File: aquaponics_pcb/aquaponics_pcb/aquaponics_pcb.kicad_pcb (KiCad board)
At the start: 2 copper layers, 60.5 x 73.5 mm, 67 parts, among them IC1 AZ1117CH-3.3TRG1, IC2 ESP32-S3-WROOM-1U-N8, IC3 ADM3260ARSZ, IC4 DRV8214RTER, IC5 DRV8214RTER, J1 RFPC-SMA27-F, J2 2338792-1, J3 RFPC-SMA27-F, J4 RFPC-SMA27-F, J5 Screw_Terminal_01x02, J6 Screw_Terminal_01x02, Q1 SSM6N35AFE,LF, Q2 SSM6N35AFE,LF, U1 Atlas Scientific EZO, U2 Atlas Scientific EZO, U3 Atlas Scientific EZO

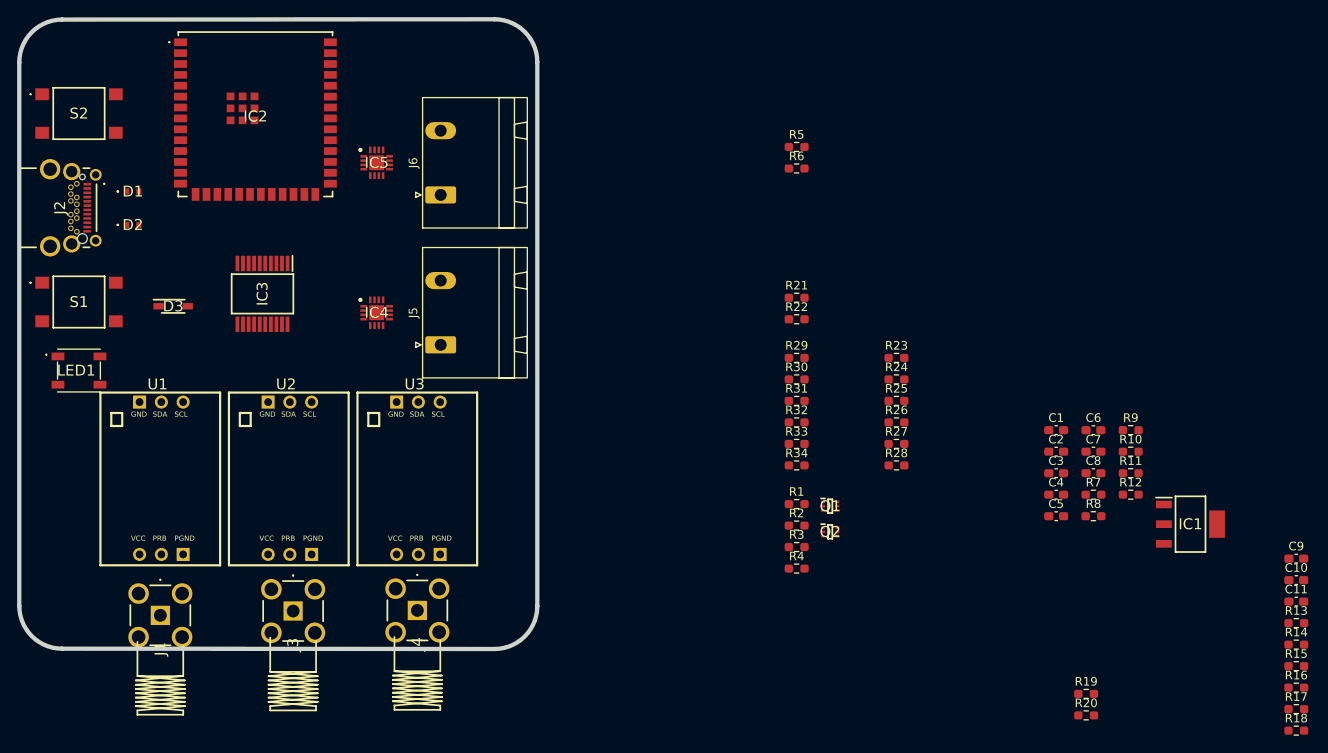
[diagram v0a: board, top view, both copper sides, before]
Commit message: Update PCB: add ADM3260, replace C3 with SMA connector
Replaced C3 capacitor footprint with an RFPC-SMA27-F SMA connector and added the ADM3260ARSZ digital isolator (IC3) to the PCB. Updated R3 to a 10k resistor and made related netlist and footprint changes.
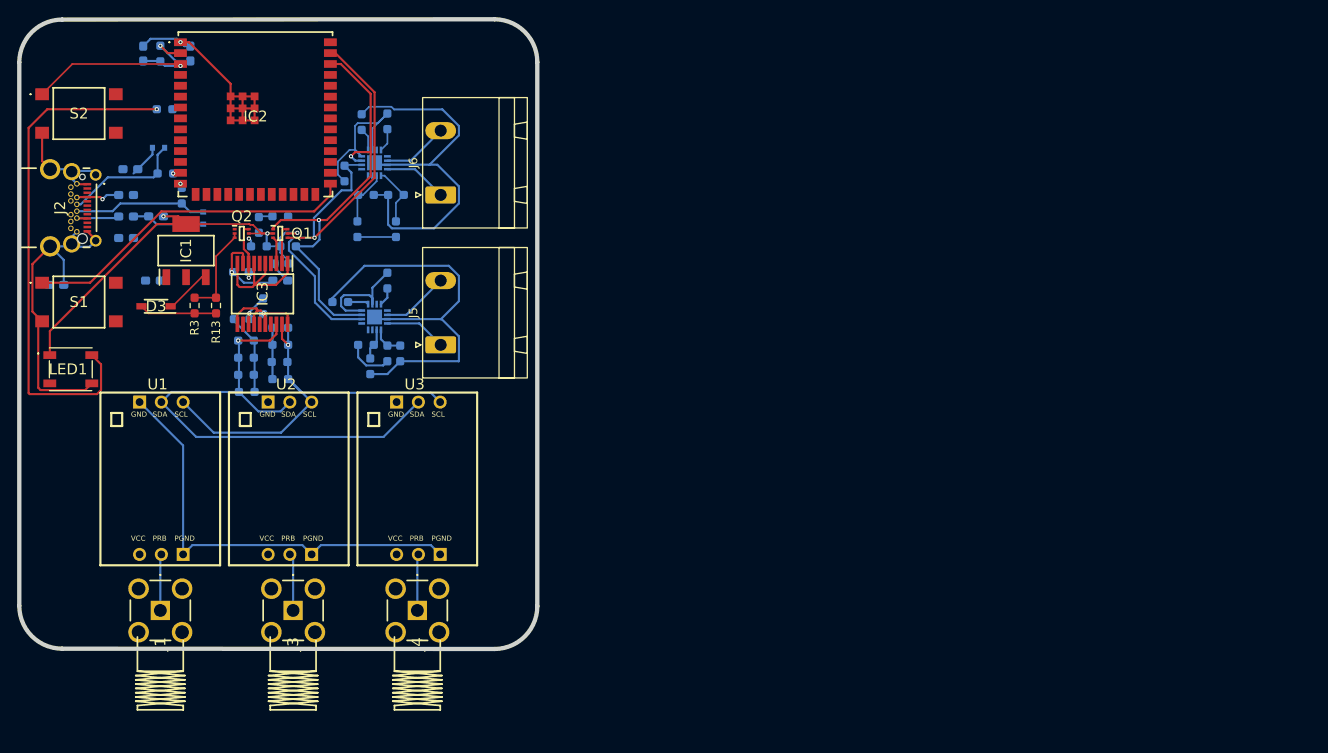
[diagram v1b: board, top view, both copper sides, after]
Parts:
- C1, C10, C11, C2, C3, C4, C5, C6, C7, C8, C9, D1, D2, IC4, IC5, R1, R10, R11, R12, R14, R15, R16, R17, R18, R19, R2, R20, R21, R22, R23, R24, R25, R26, R27, R28, R29, R30, R31, R32, R33, R34, R4, R5, R6, R7, R8, R9: moved to B.Cu
- moved C11 144.6 mm to (131.5, 78.5)
- moved C10 143.0 mm to (131.5, 81.0)
- moved C9 141.6 mm to (131.5, 83.5)
- moved R13 131.4 mm to (142.0, 91.4), turned to 90 degrees
- moved R17 131.2 mm to (145.0, 93.0)
- moved R14 130.6 mm to (144.9, 87.5)
- moved R18 130.4 mm to (147.5, 91.5), turned to -90 degrees
- moved R16 127.3 mm to (145.6, 101.5), turned to 180 degrees
- moved R15 123.2 mm to (149.5, 100.0)
- moved IC1 121.5 mm to (138.5, 85.0), turned to 90 degrees
- moved R9 121.5 mm to (135.5, 62.0), turned to 90 degrees
- moved R10 119.6 mm to (136.0, 68.5), turned to 180 degrees
- moved C5 119.5 mm to (133.5, 62.0), turned to -90 degrees
- moved C4 119.2 mm to (123.4, 89.0), turned to 180 degrees
- moved R8 115.5 mm to (136.1, 76.0)
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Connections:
- U1 pad 1: GND -> Earth_Clean
- U2 pad 1: GND -> Earth_Clean
- U3 pad 1: GND -> Earth_Clean
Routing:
- net GND: track 0.00 -> 211.2 mm, vias 0 -> 1
- net V_MCU: track 0.00 -> 99.3 mm, vias 0 -> 4
- net Earth_Clean: track 0.00 -> 63.7 mm, vias 0 -> 1
- net /Cond_Subcircuit/TX_(SDA): track 0.00 -> 62.2 mm, vias 0 -> 1
- net /ESP32_MCU/I2C_0_MCU_SDA: track 0.00 -> 61.1 mm, vias 0 -> 1
- net Net-(LED1-DIN): track 0.00 -> 60.0 mm, vias 0 -> 1
- net /ESP32_MCU/I2C_0_MCU_SCL: track 0.00 -> 52.2 mm, vias 0 -> 2
- net /Cond_Subcircuit/RX_(SCL): track 0.00 -> 49.4 mm, vias 0 -> 1
- net /ESP32_MCU/GPIO0: track 0.00 -> 39.2 mm
- net +5V_USB: track 0.00 -> 32.0 mm, vias 0 -> 2
- net /ESP32_MCU/EN: track 0.00 -> 22.2 mm, vias 0 -> 1
- net Net-(J2-DP2): track 0.00 -> 15.5 mm
- net /electrical_isolator/VISO: track 0.00 -> 15.5 mm
- net Net-(J2-DN2): track 0.00 -> 14.3 mm
- net /electrical_isolator/ISO_EN: track 0.00 -> 10.9 mm
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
